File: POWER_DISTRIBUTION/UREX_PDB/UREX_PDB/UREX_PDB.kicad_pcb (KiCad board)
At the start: 4 copper layers, 90 x 60 mm, 92 parts, among them IC1 TCAN1044VDDFR, IC2 TPS1HB08BQPWPRQ1, IC3 TPS1HB08BQPWPRQ1, IC4 INA232AIDDFR, J1 S2B-PH-SM4-TB_LF__SN_, J11 Conn_01x02, J33 Conn_01x02, J34 Conn_01x02, J35 Conn_01x02, J36 Conn_01x02, J37 Conn_01x02, J4 S2B-PH-SM4-TB_LF__SN_, J5 S3B-PH-SM4-TB_LF__SN_, J6 S4B-PH-SM4-TB_LF__SN_, J7 S2B-PH-SM4-TB_LF__SN_, J8 S3B-PH-SM4-TB_LF__SN_, J9 S6B-PH-SM4-TB_LF__SN_, Q1 RSS070N05HZGTB, Q2 RSS070N05HZGTB, U6 ESP32-WROOM-32E, U7 USBLC6-2SC6

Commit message: 040722026
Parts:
- removed J35: Conn_01x02, Connector_JST:JST_PH_S2B-PH-K_1x02_P2.00mm_Horizontal
- added IC5: TPS22997RYZR, SamacSys_Parts:TPS22997RYZR, F.Cu at (105.5, 105.6)
- added J10: S2B-PH-SM4-TB_LF__SN_, SamacSys_Parts:S2BPHSM4TBLFSN, F.Cu at (112.2, 118.9)
- C1, C2, C3, C4, C5, C6, C7, C8, G*** (x2), J6, R44, R45: moved to B.Cu
- C13, R10, R11, R12, R13, R14, R15, R16, R3, R4, R5, R6, R7, R8, R9: moved to F.Cu
- TP2, TP3, TP4, TP5, TP6: footprint TestPoint:TestPoint_Pad_2.0x2.0mm -> SamacSys_Parts:S175146R
- moved R45 31.0 mm to (128.7, 104.9)
- moved R44 31.0 mm to (128.7, 103.2)
- moved G*** 25.6 mm to (132.9, 52.2), turned to 180 degrees
- moved G*** 25.0 mm to (132.5, 60.2), turned to 180 degrees
- moved FB1 18.4 mm to (118.8, 85.8)
- moved J4 17.6 mm to (127.0, 118.8)
- moved TP6 17.5 mm to (118.9, 98.1)
- moved C51 16.2 mm to (122.6, 77.6)
- moved C52 16.2 mm to (122.6, 79.2)
- moved C12 14.9 mm to (122.4, 93.7)
- moved C18 14.8 mm to (118.0, 90.2), turned to 180 degrees
- moved C11 14.5 mm to (122.4, 92.0)
- moved C1 14.5 mm to (132.4, 94.2)
- moved C2 14.4 mm to (132.4, 92.0)
- moved C3 14.3 mm to (132.4, 89.8)
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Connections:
- J33 pad 1: VBAT_Fused_OUT -> VBAT_Fused
- J34 pad 1: VBAT_Fused_OUT -> VBAT_Fused
- J6 pad 2: PGM_TX_FILT -> PGM_RX_FILT
- J6 pad 3: PGM_RX_FILT -> PGM_TX_FILT
- PS1 pad 4: unconnected-(PS1-NC-Pad4) -> GND
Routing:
- net HEATER_EN: track 35.2 -> 72.4 mm, vias 1 -> 2
- net BOOT: track 0.74 -> 33.3 mm, vias 0 -> 2
- net GPIO2_EN: track 4.60 -> 35.4 mm, vias 0 -> 1
- net Net-(Q2-GATE): track 53.2 -> 29.6 mm, vias 1 -> 0
- net GND: track 86.7 -> 73.6 mm, vias 90 -> 96
- net VBAT_Fused: track 13.8 -> 25.9 mm, vias 1 -> 50
- net PGM_TX_FILT: track 16.8 -> 6.25 mm, vias 0 -> 1
- net Net-(D1-A): track 14.7 -> 4.34 mm, vias 1 -> 0
- net VBAT_Fused_OUT: track 10.8 -> 19.8 mm, vias 1 -> 2
- net Net-(IC2-EN): track 6.31 -> 14.3 mm, vias 1 -> 2
- net PGM_TX: track 11.7 -> 19.5 mm
- net PGM_RX_FILT: track 13.6 -> 6.51 mm, vias 0 -> 1
- net Net-(IC2-SEL1): track 7.87 -> 2.27 mm, vias 1 -> 0
- net GPIO1_EN: track 8.94 -> 3.64 mm
- net PGM_RX: track 15.0 -> 19.0 mm, vias 2 -> 0
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- added copper zone on B.Cu, net VBAT_Fused
- added copper zone on B.Cu, net VBAT_Fused_OUT
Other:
- board text added: "3v3"
- board text added: "CANH"
- board text added: "CANL"
- board text added: "GND"
- board text added: "gnd"
- board text added: "onewire1"
- board text added: "onewire2"
- board text removed: "5V"
- board text removed: "CAN"
- board text removed: "OW1"
- board text removed: "OW2"

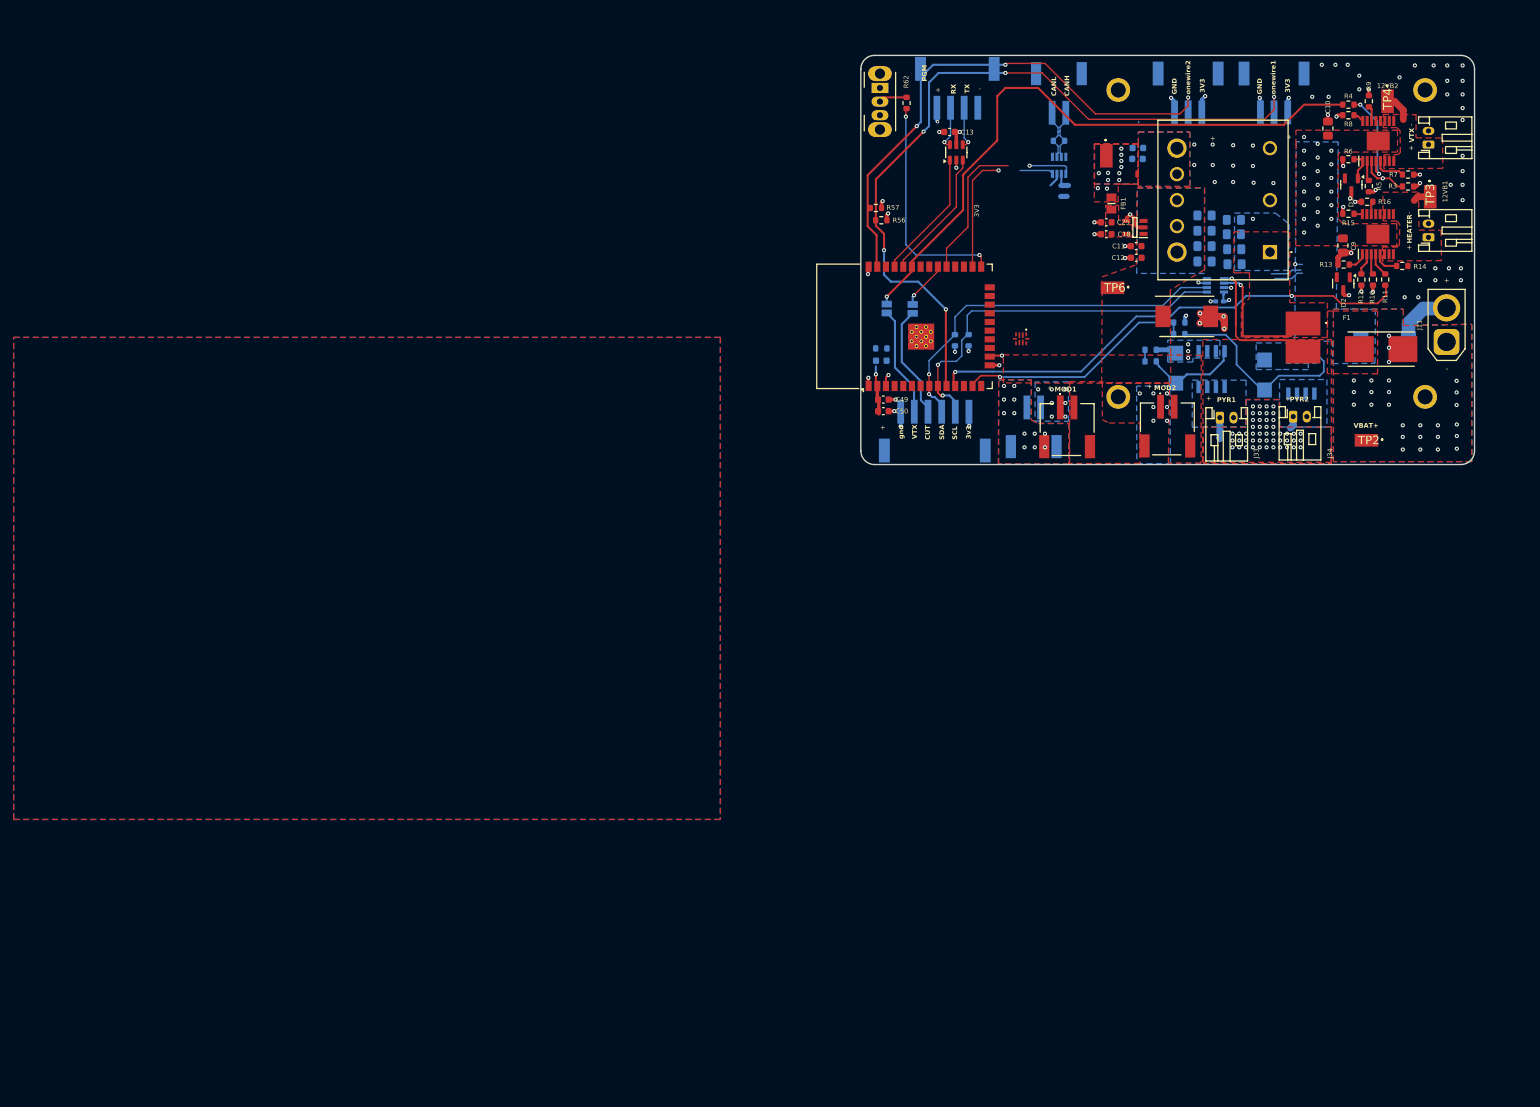
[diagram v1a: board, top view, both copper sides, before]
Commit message: Updated to shift register IC
delete VTX_EN or just do some interrupt
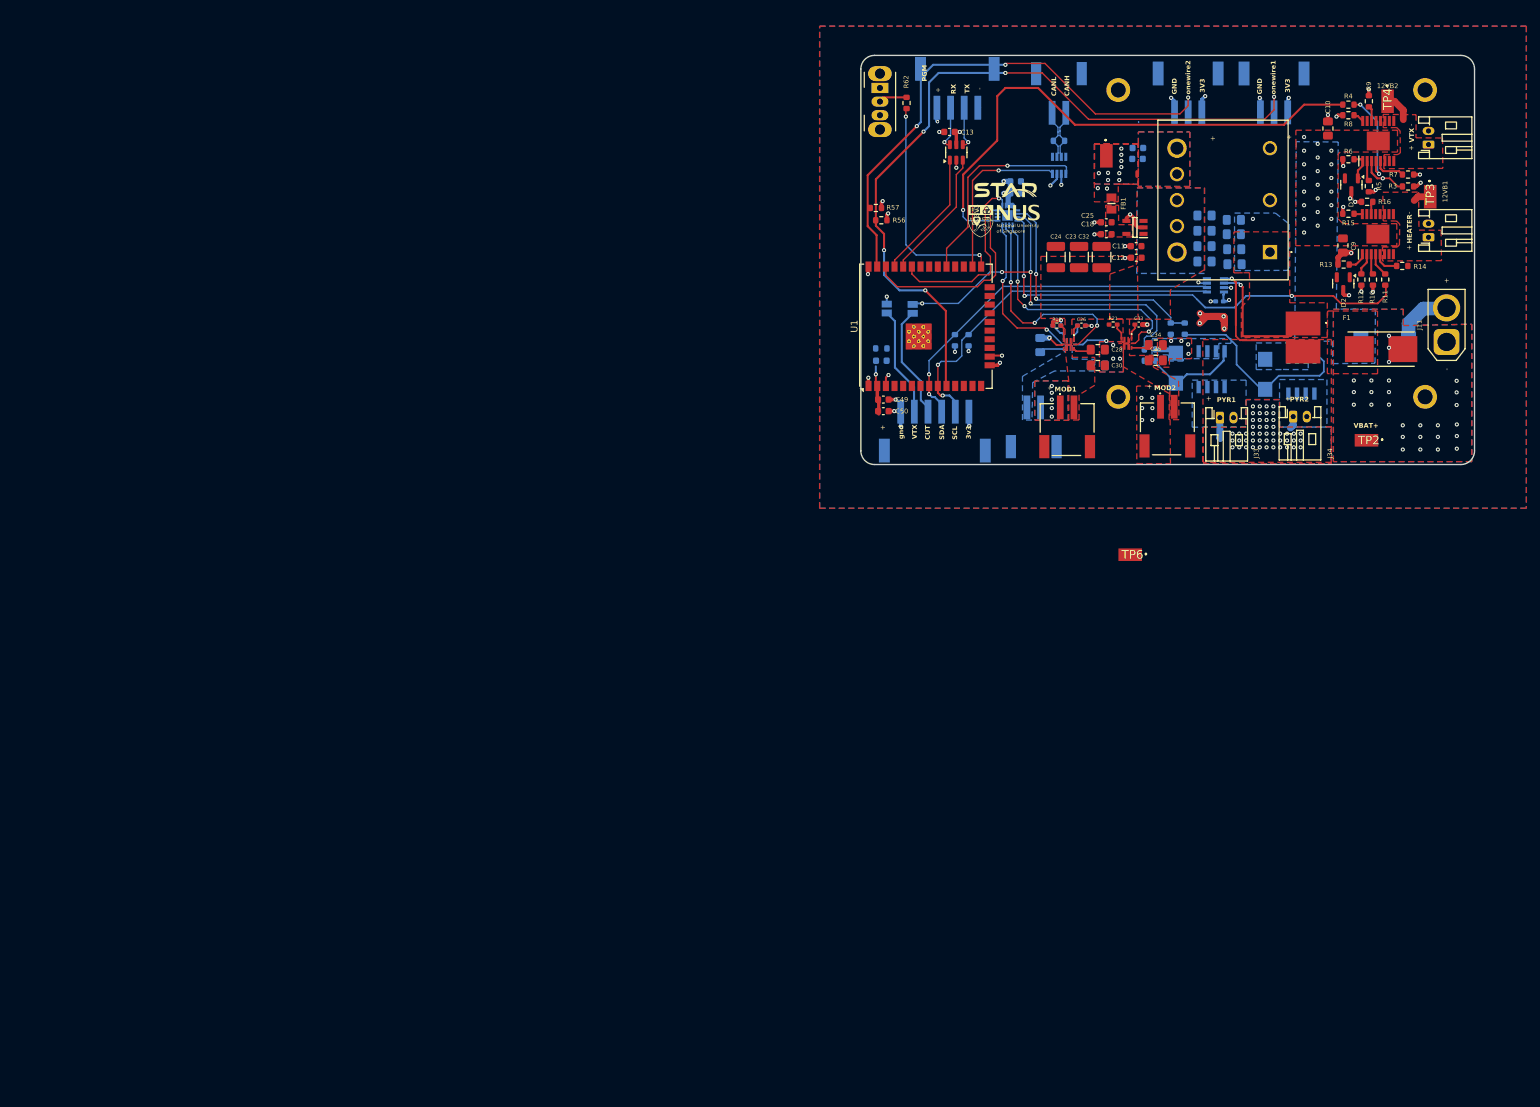
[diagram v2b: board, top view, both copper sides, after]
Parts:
- removed D8: SSC53L-E3_57T, SamacSys_Parts:DIOM7959X262N
- removed U6: ESP32-WROOM-32E, RF_Module:ESP32-WROOM-32D
- added C23: 10uF @50V, Capacitor_SMD:C_1210_3225Metric_Pad1.33x2.70mm_HandSolder, F.Cu at (114.0, 93.6)
- added C24: 10uF @50V, Capacitor_SMD:C_1210_3225Metric_Pad1.33x2.70mm_HandSolder, F.Cu at (110.6, 93.6)
- added C26: 100nF @50V, Capacitor_SMD:C_0402_1005Metric_Pad0.74x0.62mm_HandSolder, F.Cu at (114.3, 103.7)
- added C27: 100nF @50V, Capacitor_SMD:C_0402_1005Metric_Pad0.74x0.62mm_HandSolder, B.Cu at (110.8, 103.7)
- added C28: 1uF @50V, Capacitor_SMD:C_0805_2012Metric_Pad1.18x1.45mm_HandSolder, F.Cu at (116.8, 107.2)
- added C29: 1uF @50V, Capacitor_SMD:C_0805_2012Metric_Pad1.18x1.45mm_HandSolder, B.Cu at (108.3, 106.5)
- added C30: 1uF @50V, Capacitor_SMD:C_0805_2012Metric_Pad1.18x1.45mm_HandSolder, F.Cu at (116.8, 109.5)
- added C31: 1uF @50V, Capacitor_SMD:C_0805_2012Metric_Pad1.18x1.45mm_HandSolder, B.Cu at (116.8, 109.5)
- added C32: 10uF @50V, Capacitor_SMD:C_1210_3225Metric_Pad1.33x2.70mm_HandSolder, F.Cu at (117.3, 93.6)
- added C33: 100nF @50V, Capacitor_SMD:C_0402_1005Metric_Pad0.74x0.62mm_HandSolder, F.Cu at (122.8, 103.5)
- added C34: 1uF @50V, Capacitor_SMD:C_0805_2012Metric_Pad1.18x1.45mm_HandSolder, F.Cu at (125.2, 106.5)
- added C35: 1uF @50V, Capacitor_SMD:C_0805_2012Metric_Pad1.18x1.45mm_HandSolder, F.Cu at (125.2, 108.8)
- added C53: 100nF, Capacitor_SMD:C_0603_1608Metric, B.Cu at (104.7, 84.2)
- added C54: 1uF, Capacitor_SMD:C_0603_1608Metric, B.Cu at (104.7, 82.5)
- added IC10: TPS22997RYZR, SamacSys_Parts:TPS22997RYZR, F.Cu at (121.0, 106.2)
- added IC8: TPS22997RYZR, SamacSys_Parts:TPS22997RYZR, F.Cu at (112.5, 106.4)
- added IC9: TPS22997RYZR, SamacSys_Parts:TPS22997RYZR, B.Cu at (112.5, 106.4)
- added R19: 10k, Resistor_SMD:R_0402_1005Metric_Pad0.72x0.64mm_HandSolder, F.Cu at (110.8, 103.7)
- added R20: 10k, Resistor_SMD:R_0402_1005Metric_Pad0.72x0.64mm_HandSolder, B.Cu at (114.3, 103.7)
- added R21: 10k, Resistor_SMD:R_0402_1005Metric_Pad0.72x0.64mm_HandSolder, F.Cu at (119.0, 103.5)
- added U1: ESP32-WROOM-32UE-R2, RF_Module:ESP32-WROOM-32UE, F.Cu at (91.5, 103.8)
- G*** (x2): moved to F.Cu
- IC5: value TPS22997RYZR -> TCA6408ARGTR; footprint SamacSys_Parts:TPS22997RYZR -> SamacSys_Parts:QFN50P300X300X100-17N-D; moved to B.Cu
- moved G*** 41.2 mm to (103.0, 80.6), turned to 0 degrees
- moved G*** 40.7 mm to (103.0, 88.3), turned to 0 degrees
- moved TP6 39.2 mm to (121.5, 137.2)
- moved IC5 18.2 mm to (103.5, 87.5), turned to 180 degrees
- moved R44 1.54 mm to (127.5, 104.1), turned to 90 degrees
- moved R45 1.13 mm to (129.5, 104.1), turned to 90 degrees
- moved D9 0.14 mm to (141.3, 110.8)
- moved R43 0.14 mm to (124.4, 108.8)
- moved R42 0.11 mm to (124.4, 107.2)
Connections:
- IC5 pad 1: unconnected-(IC5-VBIAS-Pad1) -> GPIO_RST
- IC5 pad 2: unconnected-(IC5-VIN_1-Pad2) -> GPIO2_EN
- IC5 pad 3: unconnected-(IC5-VIN_2-Pad3) -> GPIO1_EN
- IC5 pad 4: unconnected-(IC5-PG-Pad4) -> HEATER_EN
- IC5 pad 5: unconnected-(IC5-GND-Pad5) -> 5VDC_BUS3_EN
- IC5 pad 6: unconnected-(IC5-QOD-Pad6) -> GND
- IC5 pad 7: unconnected-(IC5-VOUT_1-Pad7) -> 5VDC_BUS1_EN
- IC5 pad 8: unconnected-(IC5-VOUT_2-Pad8) -> 5VDC_BUS2_EN
- IC5 pad 9: unconnected-(IC5-CT-Pad9) -> VTX_EN
- J10 pad 2: +5V0 -> 5VDC_BUS1
- J4 pad 2: +5V0 -> 5VDC_BUS3
- J7 pad 2: +5V0 -> 5VDC_BUS2
- JP4 pad 1: CUTTER_EN -> GPIO1_EN
- PS1 pad 4: GND -> unconnected-(PS1-NC-Pad4)
- TP6 pad 1: +5V0 -> 5VDC_BUS3
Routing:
- net GPIO1_EN: track 3.64 -> 58.7 mm, vias 1 -> 4
- net 5VDC_BUS3_EN: track 0.00 -> 37.6 mm, vias 0 -> 3
- net 5VDC_BUS1_EN: track 0.00 -> 32.4 mm, vias 0 -> 3
- net I2C_SDL: track 0.00 -> 30.5 mm, vias 0 -> 1
- net I2C_SDA: track 0.00 -> 27.7 mm, vias 0 -> 1
- net 5VDC_BUS2_EN: track 0.00 -> 24.3 mm, vias 0 -> 2
- net VTX_EN: track 91.8 -> 80.8 mm, vias 1 -> 2
- net (no net): track 0.00 -> 10.2 mm, vias 0 -> 4
- net GND: track 73.6 -> 64.6 mm, vias 96 -> 53
- net CUTTER_EN: track 7.70 -> 0.00 mm, vias 1 -> 0
- net +3V3: track 27.9 -> 34.1 mm
- net I2C2_SDL: track 60.9 -> 54.9 mm
- net I2C2_SDA: track 60.5 -> 54.6 mm
- net +3.3V: track 0.00 -> 5.19 mm, vias 0 -> 3
- net unconnected-(PS1-NC-Pad4): track 0.00 -> 4.38 mm, vias 0 -> 1
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- added copper zone on B.Cu, net 5VDC_BUS1
- added copper zone on F.Cu, net 5VDC_BUS1
- added copper zone on B.Cu, net 5VDC_BUS2
- added copper zone on F.Cu, net 5VDC_BUS3

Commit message: LAYOUT FINISHED, DRC NEXT
LESO
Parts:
- added TP7: TestPoint, TestPoint:TestPoint_THTPad_1.0x1.0mm_Drill0.5mm, B.Cu at (113.6, 119.0)
- added TP8: TestPoint, TestPoint:TestPoint_THTPad_1.0x1.0mm_Drill0.5mm, F.Cu at (104.4, 116.1)
- TP2, TP3, TP4, TP5: footprint SamacSys_Parts:S175146R -> TestPoint:TestPoint_THTPad_1.0x1.0mm_Drill0.5mm
- TP6: footprint SamacSys_Parts:S175146R -> TestPoint:TestPoint_THTPad_1.0x1.0mm_Drill0.5mm; moved to B.Cu
- moved TP6 19.4 mm to (127.9, 118.9), turned to 180 degrees
- moved G*** 8.12 mm to (94.9, 80.9)
- moved G*** 7.70 mm to (95.3, 88.3)
- moved C48 2.02 mm to (83.5, 107.5), turned to -90 degrees
- moved C24 1.41 mm to (110.4, 95.0)
- moved C23 1.40 mm to (113.9, 95.0)
- moved C32 1.40 mm to (117.3, 95.0)
- moved Q1 0.95 mm to (133.4, 111.0)
- moved R53 0.56 mm to (85.2, 107.5), turned to -90 degrees
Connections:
- PS1 pad 4: unconnected-(PS1-NC-Pad4) -> GND
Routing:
- net GPIO_RST: track 1.32 -> 26.4 mm, vias 0 -> 3
- net VTX_EN: track 80.8 -> 105.3 mm
- net GPIO_INT: track 0.00 -> 17.2 mm, vias 0 -> 1
- net GND: track 64.6 -> 79.1 mm, vias 53 -> 83
- net (no net): track 10.2 -> 0.00 mm, vias 4 -> 0
- net unconnected-(PS1-NC-Pad4): track 4.38 -> 0.00 mm, vias 1 -> 0
- net +3V3: track 34.1 -> 38.1 mm, vias 25 -> 26
- net 5VDC_BUS1: track 0.00 -> 3.49 mm
- net 5VDC_BUS3: track 0.00 -> 3.37 mm
- net 5VDC_BUS2: track 0.00 -> 2.14 mm
- net I2C_SDL: track 30.5 -> 31.5 mm
- net +3.3V: track 5.19 -> 6.13 mm, vias 3 -> 4
- net Net-(Q1-GATE): track 13.6 -> 12.8 mm
- net VBAT_Fused_OUT: track 19.8 -> 19.1 mm
- net Net-(Q2-GATE): track 29.6 -> 29.1 mm
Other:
- board text added: "3V3 TP"
- board text added: "POWER DISTRIBUTION BOARD"
- board text removed: "UREx Weather Balloon"

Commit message: First Production
Rev1.0 sent for production
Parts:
- TP2, TP3, TP4, TP5: footprint TestPoint:TestPoint_THTPad_1.0x1.0mm_Drill0.5mm -> TestPoint:TestPoint_Pad_1.5x1.5mm
- TP6, TP7: footprint TestPoint:TestPoint_THTPad_1.0x1.0mm_Drill0.5mm -> TestPoint:TestPoint_Pad_1.5x1.5mm; moved to F.Cu
- TP8: footprint TestPoint:TestPoint_THTPad_1.0x1.0mm_Drill0.5mm -> TestPoint:TestPoint_Pad_1.5x1.5mm; moved to B.Cu
- moved TP6 7.60 mm to (127.9, 111.3), turned to 0 degrees
- moved TP7 5.23 mm to (118.8, 118.4), turned to 0 degrees
- moved R2 0.26 mm to (111.1, 76.3)
- moved C5 0.15 mm to (136.7, 88.0)
- moved J6 0.10 mm to (99.2, 71.8)
- turned TP8 to 180 degrees
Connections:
- C26 pad 1: +3.3V -> +3V3
- C27 pad 1: +3.3V -> +3V3
- C33 pad 1: +3.3V -> +3V3
- R19 pad 1: +3.3V -> +3V3
- R20 pad 1: +3.3V -> +3V3
- R21 pad 1: +3.3V -> +3V3
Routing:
- net +3.3V: track 6.13 -> 0.00 mm, vias 4 -> 0
- net +3V3: track 38.1 -> 43.2 mm, vias 26 -> 30
- net 5VDC_BUS3: track 3.37 -> 0.07 mm
- net 5VDC_BUS1: track 3.49 -> 6.69 mm
- net I2C2_SDL: track 55.2 -> 52.8 mm
- net I2C2_SDA: track 55.0 -> 52.9 mm
- net unconnected-(U1-IO13-Pad16): track 1.94 -> 0.00 mm, vias 1 -> 0
- net GND: track 79.1 -> 77.5 mm
- net CUTTER_EN_EXT: track 17.6 -> 16.0 mm
- net CAN-: track 7.44 -> 6.06 mm
- net CAN+: track 7.42 -> 6.06 mm
- net GPIO_RST: track 26.4 -> 25.1 mm
- net unconnected-(H8-Pad1): track 1.27 -> 0.00 mm
- net onewire2: track 78.5 -> 77.3 mm
- net onewire1: track 112.9 -> 112.0 mm
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
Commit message: production uipdate
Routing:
- net +3V3: track 43.2 -> 48.5 mm, vias 30 -> 34
- net Net-(D2-A): track 2.32 -> 4.21 mm
- net GPIO1_EN: track 58.7 -> 60.4 mm
- net GND: vias 83 -> 151
- net +5V0: vias 0 -> 2
- removed copper zone on B.Cu, net 5VDC_BUS1
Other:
- board text added: "12VB1_EN"
- board text added: "PYR1_EN"
- board text added: "PYR_EN"
- board text added: "bridge to override MCU control"
- board text removed: "CUT"
- board text removed: "HEATER"
- board text removed: "VTX"
